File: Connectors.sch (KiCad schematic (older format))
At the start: 16 parts, among them J1 Conn_01x02, J10 Conn_01x08, J11 Conn_01x03, J12 Conn_01x02, J14 Conn_01x04, J15 Conn_01x04, J16 Conn_01x01, J17 Conn_01x04, J2 Conn_01x04, J3 Conn_01x04, J4 Conn_01x03, J6 Conn_01x06, J7 Conn_01x06, J8 Conn_01x04, J9 Conn_01x08

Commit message: Small cleanups
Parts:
- gave numbers to parts that had none: 1
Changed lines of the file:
@@
 P 2650 3750
 AR Path="/608E6C63" Ref="J?"  Part="1"
-AR Path="/60A7361B/608E6C63" Ref="J?"  Part="1"
-F 0 "J?" H 2730 3792 50  0000 L CNN
+AR Path="/60A7361B/608E6C63" Ref="J5"  Part="1"
+F 0 "J5" H 2730 3792 50  0000 L CNN
 F 1 "Conn_01x03" H 2400 3550 50  0000 L CNN
 F 2 "Connector_Wire:SolderWire-0.1sqmm_1x03_P3.6mm_D0.4mm_OD1mm" H 2650 3750 50  0001 C CNN

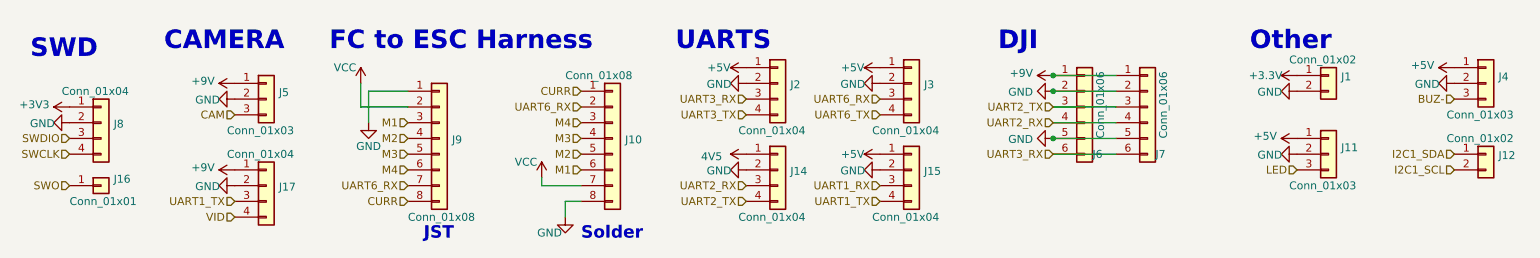
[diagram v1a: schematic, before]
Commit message: Changed to 20x20 form factor
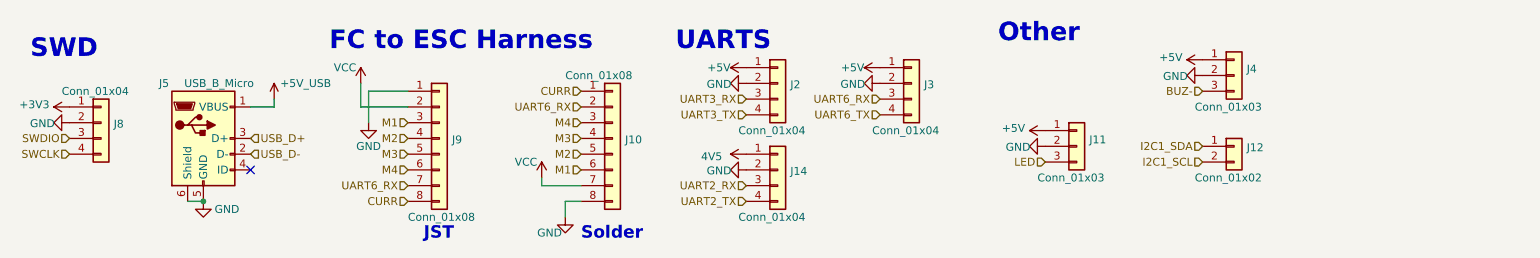
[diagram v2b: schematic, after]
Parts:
- removed J1: Conn_01x02, Connector_Wire:SolderWire-0.1sqmm_1x02_P3.6mm_D0.4mm_OD1mm, symbol Connector_Generic:Conn_01x02
- removed J15, J17: Conn_01x04, Connector_Wire:SolderWire-0.1sqmm_1x04_P3.6mm_D0.4mm_OD1mm, symbol Connector_Generic:Conn_01x04
- removed J16: Conn_01x01, Connector_Wire:SolderWire-0.1sqmm_1x01_D0.4mm_OD1mm, symbol Connector_Generic:Conn_01x01
- removed J5: Conn_01x03, Connector_Wire:SolderWire-0.1sqmm_1x03_P3.6mm_D0.4mm_OD1mm, symbol Connector_Generic:Conn_01x03
- removed J6: Conn_01x06, Footprints:JST_SM06B-SRSS-TB(LF)(SN), symbol Connector_Generic:Conn_01x06
- removed J7: Conn_01x06, Connector_Wire:Connector_Wire_Solder_DJI, symbol Connector_Generic:Conn_01x06
- added J5: USB_B_Micro, Connector_USB:USB_Micro-B_GCT_USB3076-30-A, symbol Connector:USB_B_Micro
- J10: footprint Connector_Wire:SolderWire-0.1sqmm_1x08_D0.4mm_OD1mm -> Connector_Wire:Conn_FC_Solder_8
- J11, J4: footprint Connector_Wire:SolderWire-0.1sqmm_1x03_P3.6mm_D0.4mm_OD1mm -> Connector_Wire:Conn_3Pin
- J12: footprint Connector_Wire:SolderWire-0.1sqmm_1x02_P3.6mm_D0.4mm_OD1mm -> Connector_Wire:Conn_2Pin
- J14, J2, J3: footprint Connector_Wire:SolderWire-0.1sqmm_1x04_P3.6mm_D0.4mm_OD1mm -> Connector_Wire:Conn_4Pin
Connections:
- net GND: now also J5.5 (GND), J5.6 (Shield)
- new net +5V_USB: J5.1 (VBUS)
- new net USB_D+: J5.3 (D+)
- new net USB_D-: J5.2 (D-)
- no-connect marks 0 -> 1
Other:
- note removed: "CAMERA"
- note removed: "DJI"
- moved on the sheet: J11, J12, J4

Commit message: Changes made
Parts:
- removed J14, J3: Conn_01x04, Connector_Wire:Conn_4Pin, symbol Connector_Generic:Conn_01x04
- removed J4: Conn_01x03, Connector_Wire:Conn_3Pin, symbol Connector_Generic:Conn_01x03
- added J1: Conn_01x03, Connector_JST:JST_SH_SM03B-SRSS-TB_1x03-1MP_P1.00mm_Horizontal, symbol Connector_Generic:Conn_01x03
- J11: footprint Connector_Wire:Conn_3Pin -> Connector_JST:JST_SH_SM03B-SRSS-TB_1x03-1MP_P1.00mm_Horizontal
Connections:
- net +3V3: now also J1.3 (Pin_3)
- net GND: now also J1.2 (Pin_2)
- net UART2_RX: now also J1.1 (Pin_1)
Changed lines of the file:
@@
-$EndComp
-$Comp
-L Connector_Generic:Conn_01x04 J?
-U 1 1 60A86550
-P 6750 3650
-AR Path="/60A86550" Ref="J?"  Part="1"
-AR Path="/60A7361B/60A86550" Ref="J3"  Part="1"
-F 0 "J3" H 6830 3642 50  0000 L CNN
-F 1 "Conn_01x04" H 6500 3350 50  0000 L CNN
-F 2 "Connector_Wire:Conn_4Pin" H 6750 3650 50  0001 C CNN
-F 3 "~" H 6750 3650 50  0001 C CNN
-	1    6750 3650
-	1    0    0    -1
-$EndComp
-$Comp
-L power:GND #PWR?
-U 1 1 60A86558
-P 6550 3650
-AR Path="/60A86558" Ref="#PWR?"  Part="1"
-AR Path="/60A7361B/60A86558" Ref="#PWR0133"  Part="1"
-F 0 "#PWR0133" H 6550 3400 50  0001 C CNN
-F 1 "GND" V 6555 3477 50  0000 C CNN
-F 2 "" H 6550 3650 50  0001 C CNN
-F 3 "" H 6550 3650 50  0001 C CNN
-	1    6550 3650
-	0    1    1    0
 $EndComp
 $Comp
@@
 	0    -1   -1   0
 $EndComp
-$Comp
-L Connector_Generic:Conn_01x03 J?
-U 1 1 60A8657B
-P 8800 3600
-AR Path="/60A8657B" Ref="J?"  Part="1"
-AR Path="/60A7361B/60A8657B" Ref="J4"  Part="1"
-F 0 "J4" H 8880 3642 50  0000 L CNN
-F 1 "Conn_01x03" H 8550 3400 50  0000 L CNN
-F 2 "Connector_Wire:Conn_3Pin" H 8800 3600 50  0001 C CNN
-F 3 "~" H 8800 3600 50  0000 C CNN
-	1    8800 3600
-	1    0    0    -1
-$EndComp
-$Comp
-L power:+5V #PWR?
-U 1 1 60A86581
-P 8600 3500
-AR Path="/60A86581" Ref="#PWR?"  Part="1"
-AR Path="/60A7361B/60A86581" Ref="#PWR0135"  Part="1"
-F 0 "#PWR0135" H 8600 3350 50  0001 C CNN
-F 1 "+5V" V 8615 3628 50  0000 L CNN
-F 2 "" H 8600 3500 50  0001 C CNN
-F 3 "" H 8600 3500 50  0001 C CNN
-	1    8600 3500
-	0    -1   -1   0
-$EndComp
-$Comp
-L power:GND #PWR?
-U 1 1 60A86587
-P 8600 3600
-AR Path="/60A86587" Ref="#PWR?"  Part="1"
-AR Path="/60A7361B/60A86587" Ref="#PWR0136"  Part="1"
-F 0 "#PWR0136" H 8600 3350 50  0001 C CNN
-F 1 "GND" V 8605 3427 50  0000 C CNN
-F 2 "" H 8600 3600 50  0001 C CNN
-F 3 "" H 8600 3600 50  0001 C CNN
-	1    8600 3600
-	0    1    1    0
-$EndComp
 Text Notes 3050 3450 0    118  ~ 24
 FC to ESC Harness
@@
 $EndComp
 $Comp
-L Connector_Generic:Conn_01x04 J?
-U 1 1 60A865F3
-P 5900 4200
-AR Path="/60A865F3" Ref="J?"  Part="1"
-AR Path="/60A7361B/60A865F3" Ref="J14"  Part="1"
-F 0 "J14" H 5980 4192 50  0000 L CNN
-F 1 "Conn_01x04" H 5650 3900 50  0000 L CNN
-F 2 "Connector_Wire:Conn_4Pin" H 5900 4200 50  0001 C CNN
-F 3 "~" H 5900 4200 50  0001 C CNN
-	1    5900 4200
-	1    0    0    -1
-$EndComp
-$Comp
 L power:GND #PWR?
 U 1 1 60A865FB
@@
 	1    5700 4200
 	0    1    1    0
-$EndComp
-$Comp
-L power:+5V #PWR?
-U 1 1 60A86601
-P 6550 3550
-AR Path="/60A86601" Ref="#PWR?"  Part="1"
-AR Path="/60A7361B/60A86601" Ref="#PWR0145"  Part="1"
-F 0 "#PWR0145" H 6550 3400 50  0001 C CNN
-F 1 "+5V" V 6550 3650 50  0000 L CNN
-F 2 "" H 6550 3550 50  0001 C CNN
-F 3 "" H 6550 3550 50  0001 C CNN
-	1    6550 3550
-	0    -1   -1   0
 $EndComp
 $Comp
@@
 F 0 "J11" H 7880 4092 50  0000 L CNN
 F 1 "Conn_01x03" H 7550 3850 50  0000 L CNN
-F 2 "Connector_Wire:Conn_3Pin" H 7800 4050 50  0001 C CNN
+F 2 "Connector_JST:JST_SH_SM03B-SRSS-TB_1x03-1MP_P1.00mm_Horizontal" H 7800 4050 50  0001 C CNN
 F 3 "~" H 7800 4050 50  0001 C CNN
 	1    7800 4050
@@
 	0    1    1    0
 $EndComp
-$Comp
-L power:4V5 #PWR?
-U 1 1 60A8662E
-P 5750 4100
-AR Path="/60A8662E" Ref="#PWR?"  Part="1"
-AR Path="/60A7361B/60A8662E" Ref="#PWR0150"  Part="1"
-F 0 "#PWR0150" H 5925 4175 50  0001 C CNN
-F 1 "4V5" V 5735 4303 50  0000 L CNN
-F 2 "" H 5750 4100 50  0001 C CNN
-F 3 "" H 5750 4100 50  0001 C CNN
-	1    5750 4100
-	0    -1   -1   0
-$EndComp
 Text HLabel 8600 4050 0    50   Input ~ 0
 I2C1_SDA
@@
 Text HLabel 1400 4000 0    50   Input ~ 0
 SWDIO
-Text HLabel 8600 3700 0    50   Input ~ 0
-BUZ-
 Text HLabel 7600 4150 0    50   Input ~ 0
 LED
@@
 Text HLabel 5700 3850 0    50   Input ~ 0
 UART3_TX
-Text HLabel 5700 4300 0    50   Input ~ 0
+Text HLabel 5700 4100 0    50   Input ~ 0
 UART2_RX
-Text HLabel 5700 4400 0    50   Input ~ 0
-UART2_TX
-Text HLabel 6550 3850 0    50   Input ~ 0
-UART6_TX
-Text HLabel 6550 3750 0    50   Input ~ 0
-UART6_RX
 $Comp
 L power:GND #PWR?
@@
 Text HLabel 2550 4100 2    50   Input ~ 0
 USB_D-
+$Comp
+L Connector_Generic:Conn_01x03 J1
+U 1 1 60D627E8
+P 5900 4200
+F 0 "J1" H 5980 4242 50  0000 L CNN
+F 1 "Conn_01x03" H 5980 4151 50  0000 L CNN
+F 2 "Connector_JST:JST_SH_SM03B-SRSS-TB_1x03-1MP_P1.00mm_Horizontal" H 5900 4200 50  0001 C CNN
+F 3 "~" H 5900 4200 50  0001 C CNN
+	1    5900 4200
+	1    0    0    -1
+$EndComp
+$Comp
+L power:+3V3 #PWR0104
+U 1 1 60D9A4F8
+P 5700 4300
+F 0 "#PWR0104" H 5700 4150 50  0001 C CNN
+F 1 "+3V3" V 5715 4428 50  0000 L CNN
+F 2 "" H 5700 4300 50  0001 C CNN
+F 3 "" H 5700 4300 50  0001 C CNN
+	1    5700 4300
+	0    -1   -1   0
+$EndComp
 $EndSCHEMATC

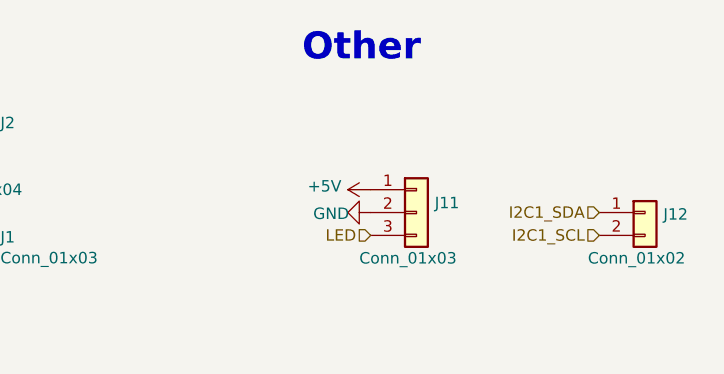
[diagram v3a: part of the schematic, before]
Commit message: Changed some components to match what is in stock
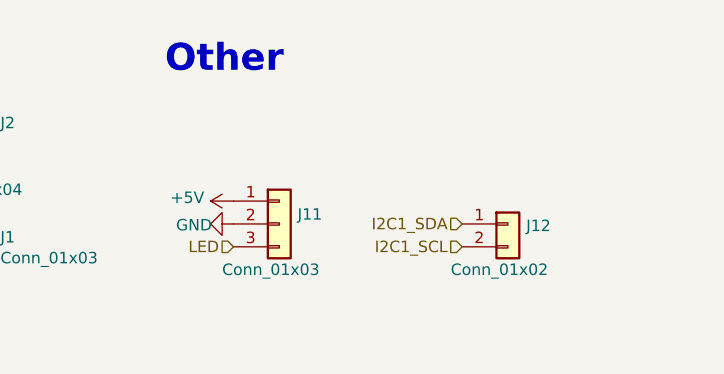
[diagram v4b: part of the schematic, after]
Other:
- moved on the sheet: J11, J12
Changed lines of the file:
@@
 L Connector_Generic:Conn_01x02 J?
 U 1 1 60A86544
-P 8800 4050
+P 8200 4100
 AR Path="/60A86544" Ref="J?"  Part="1"
 AR Path="/60A7361B/60A86544" Ref="J12"  Part="1"
-F 0 "J12" H 8880 4042 50  0000 L CNN
-F 1 "Conn_01x02" H 8550 3850 50  0000 L CNN
-F 2 "Connector_Wire:Conn_2Pin" H 8800 4050 50  0001 C CNN
-F 3 "~" H 8800 4050 50  0001 C CNN
-	1    8800 4050
+F 0 "J12" H 8280 4092 50  0000 L CNN
+F 1 "Conn_01x02" H 7950 3900 50  0000 L CNN
+F 2 "Connector_Wire:Conn_2Pin" H 8200 4100 50  0001 C CNN
+F 3 "~" H 8200 4100 50  0001 C CNN
+	1    8200 4100
 	1    0    0    -1
 $EndComp
@@
 L Connector_Generic:Conn_01x03 J?
 U 1 1 60A8661B
-P 7800 4050
+P 7200 4100
 AR Path="/60A8661B" Ref="J?"  Part="1"
 AR Path="/60A7361B/60A8661B" Ref="J11"  Part="1"
-F 0 "J11" H 7880 4092 50  0000 L CNN
-F 1 "Conn_01x03" H 7550 3850 50  0000 L CNN
-F 2 "Connector_JST:JST_SH_SM03B-SRSS-TB_1x03-1MP_P1.00mm_Horizontal" H 7800 4050 50  0001 C CNN
-F 3 "~" H 7800 4050 50  0001 C CNN
-	1    7800 4050
+F 0 "J11" H 7280 4142 50  0000 L CNN
+F 1 "Conn_01x03" H 6950 3900 50  0000 L CNN
+F 2 "Connector_JST:JST_SH_SM03B-SRSS-TB_1x03-1MP_P1.00mm_Horizontal" H 7200 4100 50  0001 C CNN
+F 3 "~" H 7200 4100 50  0001 C CNN
+	1    7200 4100
 	1    0    0    -1
 $EndComp
@@
 L power:+5V #PWR?
 U 1 1 60A86621
-P 7600 3950
+P 7000 4000
 AR Path="/60A86621" Ref="#PWR?"  Part="1"
 AR Path="/60A7361B/60A86621" Ref="#PWR0148"  Part="1"
-F 0 "#PWR0148" H 7600 3800 50  0001 C CNN
-F 1 "+5V" V 7615 4078 50  0000 L CNN
-F 2 "" H 7600 3950 50  0001 C CNN
-F 3 "" H 7600 3950 50  0001 C CNN
-	1    7600 3950
+F 0 "#PWR0148" H 7000 3850 50  0001 C CNN
+F 1 "+5V" V 7015 4128 50  0000 L CNN
+F 2 "" H 7000 4000 50  0001 C CNN
+F 3 "" H 7000 4000 50  0001 C CNN
+	1    7000 4000
 	0    -1   -1   0
 $EndComp
@@
 L power:GND #PWR?
 U 1 1 60A86627
-P 7600 4050
+P 7000 4100
 AR Path="/60A86627" Ref="#PWR?"  Part="1"
 AR Path="/60A7361B/60A86627" Ref="#PWR0149"  Part="1"
-F 0 "#PWR0149" H 7600 3800 50  0001 C CNN
-F 1 "GND" V 7605 3877 50  0000 C CNN
-F 2 "" H 7600 4050 50  0001 C CNN
-F 3 "" H 7600 4050 50  0001 C CNN
-	1    7600 4050
-	0    1    1    0
-$EndComp
-Text HLabel 8600 4050 0    50   Input ~ 0
+F 0 "#PWR0149" H 7000 3850 50  0001 C CNN
+F 1 "GND" V 7005 3927 50  0000 C CNN
+F 2 "" H 7000 4100 50  0001 C CNN
+F 3 "" H 7000 4100 50  0001 C CNN
+	1    7000 4100
+	0    1    1    0
+$EndComp
+Text HLabel 8000 4100 0    50   Input ~ 0
 I2C1_SDA
-Text HLabel 8600 4150 0    50   Input ~ 0
+Text HLabel 8000 4200 0    50   Input ~ 0
 I2C1_SCL
 Text HLabel 1400 4100 0    50   Input ~ 0
@@
 Text HLabel 1400 4000 0    50   Input ~ 0
 SWDIO
-Text HLabel 7600 4150 0    50   Input ~ 0
+Text HLabel 7000 4200 0    50   Input ~ 0
 LED
 Text HLabel 5700 3750 0    50   Input ~ 0
@@
 Text Notes 1150 3500 0    118  ~ 24
 SWD
-Text Notes 7300 3400 0    118  ~ 24
+Text Notes 6700 3450 0    118  ~ 24
 Other
 Text Notes 3650 4650 0    79   ~ 16
